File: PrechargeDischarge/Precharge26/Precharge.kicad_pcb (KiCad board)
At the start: 2 copper layers, 133 x 98 mm, 121 parts, among them J1 MicroFit, J2 Mini-Fit_Jr_5566-04A, J3 Micro-Fit 43045-0212, K1 OMRON-G2RL-24, K2 G7L-2A-X-L, Q1 2N7002, Q2 MMBT3906, Q3 2N7002, U1 TJA1051T-3, U10 LM393, U11 4N35, U2 SPAN02A-12, U3 Teensy4.0, U4 LM1117-5.0, U5 4N35, U6 4N35, U7 LM331, U8 LM331, U9 LM2904

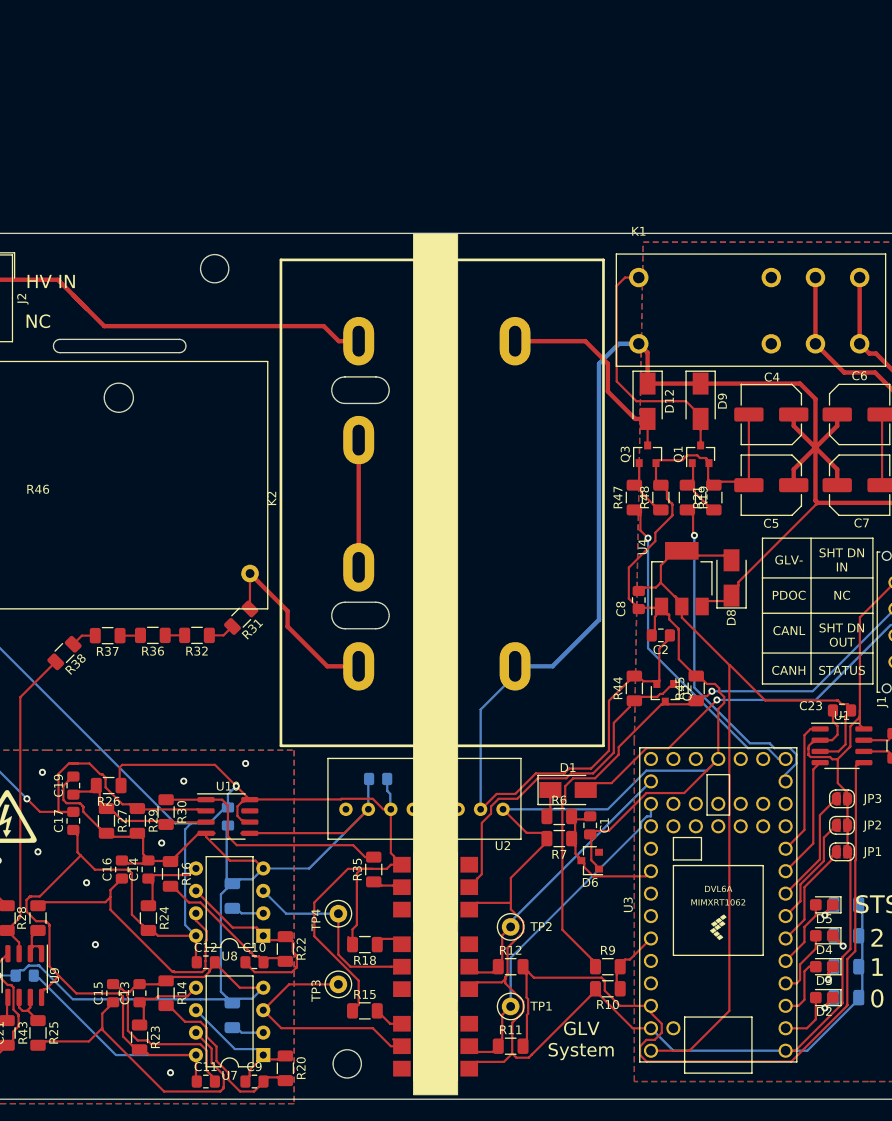
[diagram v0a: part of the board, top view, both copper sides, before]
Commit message: Precharge
Fixed Ground plane distance, added new DC converter, fixed precharge resistor value
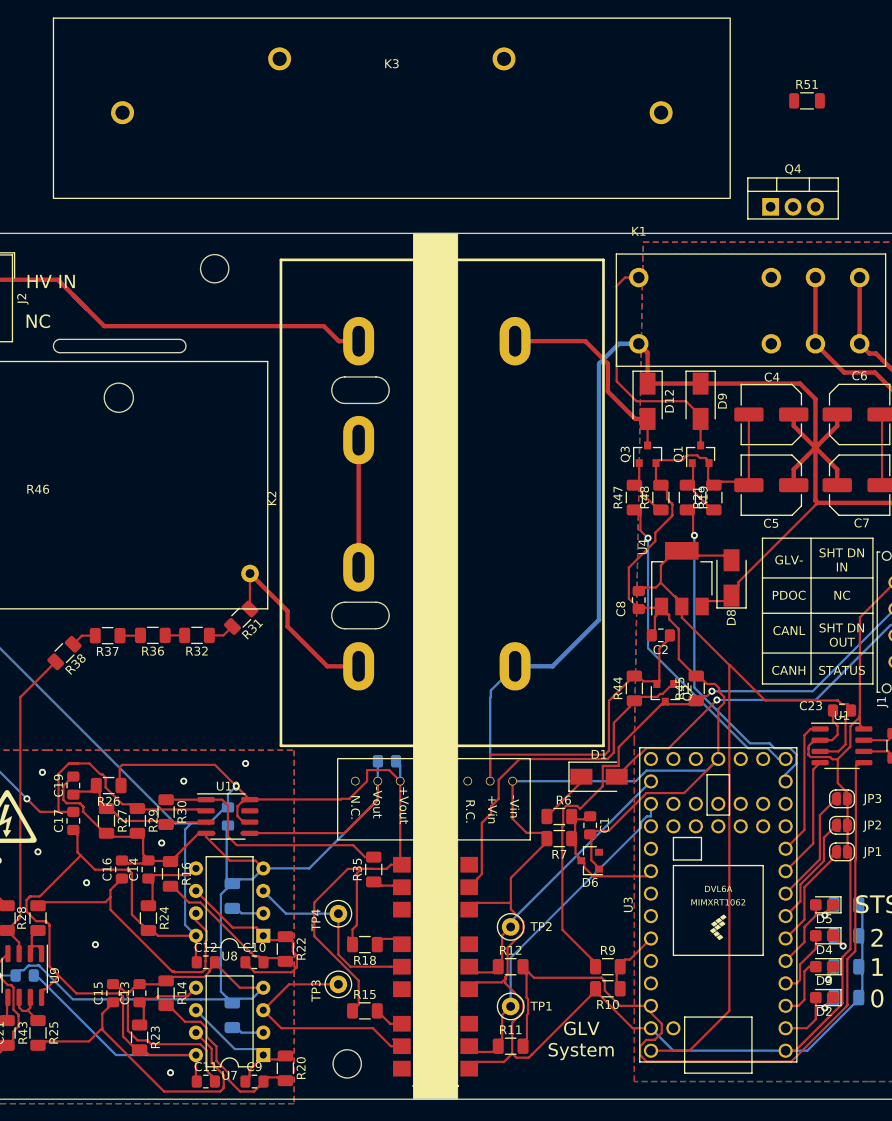
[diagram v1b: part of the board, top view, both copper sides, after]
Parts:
- added K3: Relay_SPST-NC, Library:Relay_SPST_NC_COMUS, F.Cu at (137.1, 36.3)
- added Q4: PMOS, Package_TO_SOT_THT:TO-220-3_Vertical, F.Cu at (179.9, 47.5)
- added R51: 10k, Resistor_SMD:R_1206_3216Metric, F.Cu at (184.0, 35.5)
- R46: value HSA25390RJ -> HSA253K3J
- U2: footprint Precharge:SPAN02 -> Precharge:DC-DCSPAN02W8-12
- moved D1 3.81 mm to (160.5, 112.0)
- moved C3 2.24 mm to (136.5, 110.2)
- moved U2 0.82 mm to (141.8, 114.5)
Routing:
- net GNDS: track 361.4 -> 367.4 mm
- net +12P: track 237.7 -> 242.4 mm
- net GLV+: track 92.4 -> 88.4 mm
- net +12V: track 188.0 -> 184.8 mm
- net Net-(D1-K): track 3.09 -> 6.12 mm
- net Net-(Q2-B): track 38.6 -> 39.9 mm
- net /PDOC_OK: track 68.3 -> 69.4 mm
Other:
- board text added: "5.0mm"

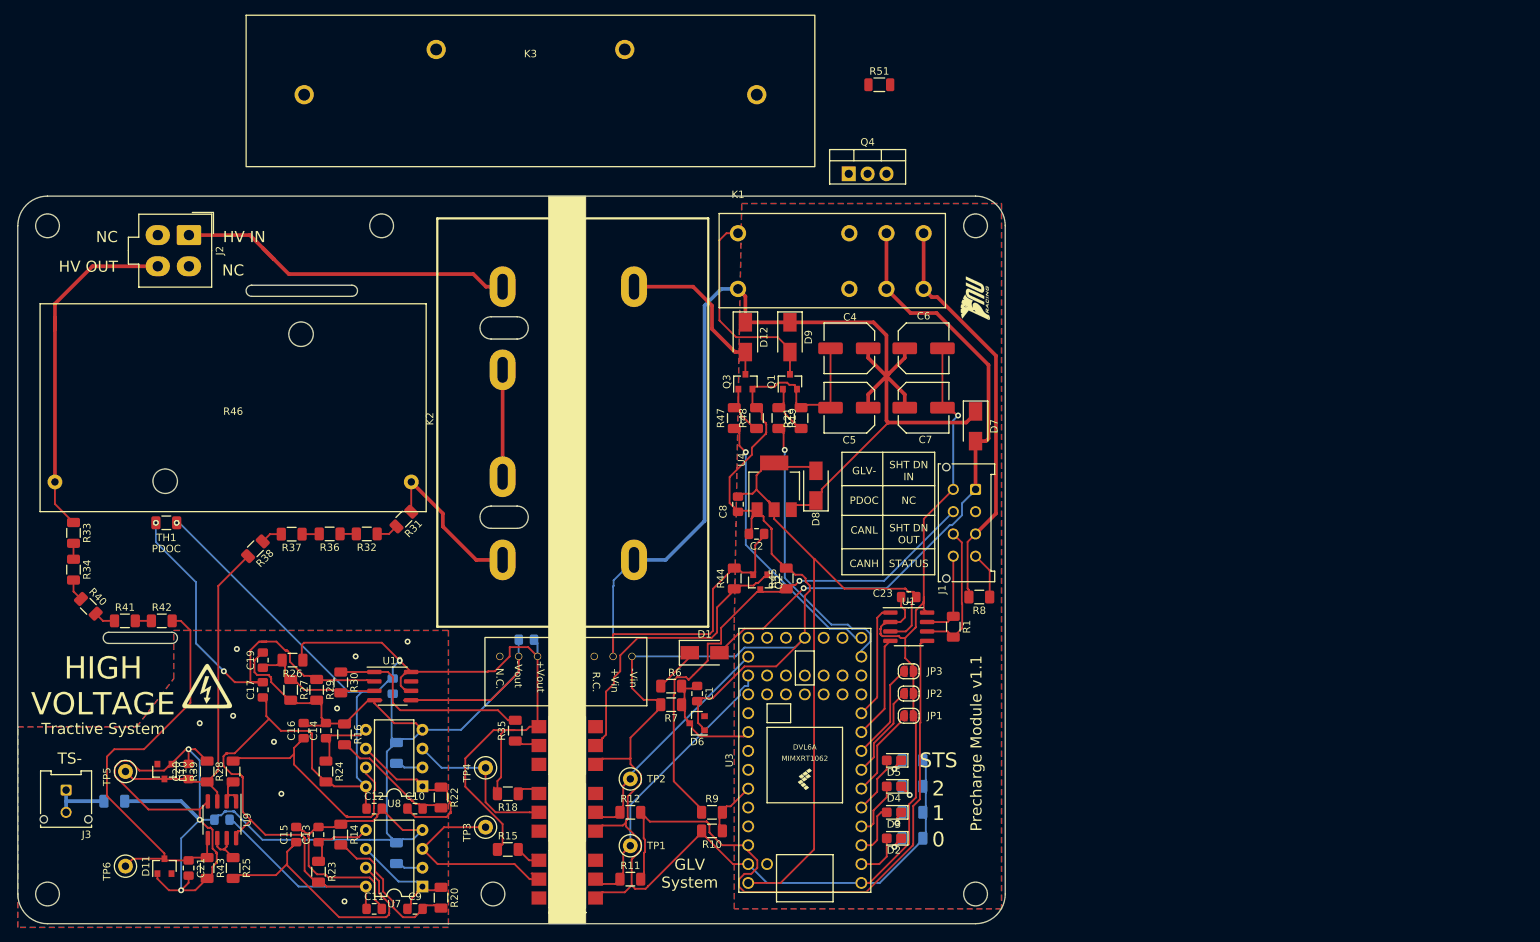
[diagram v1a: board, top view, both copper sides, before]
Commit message: added discharge relay and resistor footprints to precharge board
still need all part numbers but ffootprints are selected, go shopping on JLC
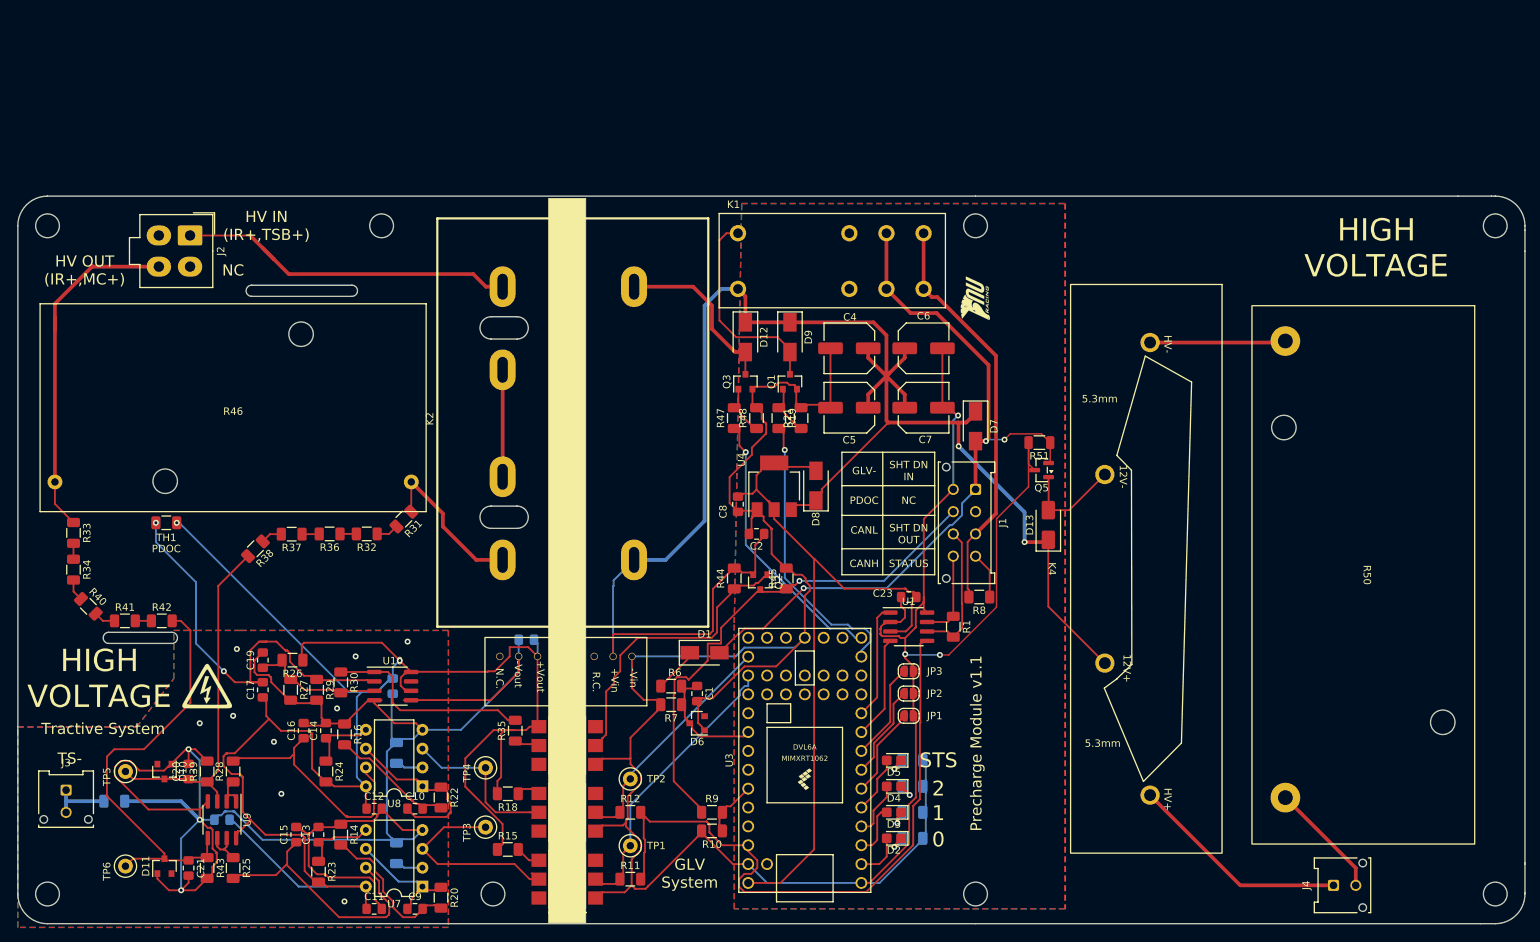
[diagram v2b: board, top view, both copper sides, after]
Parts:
- removed K3: Relay_SPST-NC, Library:Relay_SPST_NC_COMUS
- removed Q4: PMOS, Package_TO_SOT_THT:TO-220-3_Vertical
- added ?: , , F.Cu at (267.0, 144.5)
- added ?: , , F.Cu at (267.0, 54.5)
- added D13: D, Diode_SMD:D_SMA, F.Cu at (206.8, 94.8)
- added J4: Micro-Fit 43045-0212, Connector_Molex:Molex_Micro-Fit_3.0_43045-0212_2x01_P3.00mm_Vertical, F.Cu at (245.2, 143.3)
- added K4: Relay_SPST-NC, Precharge:Discharge_relay, F.Cu at (218.8, 100.7)
- added Q5: NMOS, Package_TO_SOT_SMD:SOT-23, F.Cu at (205.9, 87.4)
- added R50: HSA503K0J, Precharge:Discharge_Resistor, F.Cu at (249.2, 101.5)
- moved R51 52.8 mm to (205.6, 83.7), turned to 180 degrees
- moved J2 0.16 mm to (91.9, 55.8)
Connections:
- J1 pad 2: (no net) -> unconnected-(J1-Pin_2-Pad2)
- J2 pad 1: Net-(J2-Pad1) -> Net-(J2-Pin_1)
- J2 pad 2: (no net) -> unconnected-(J2-Pin_2-Pad2)
- J2 pad 3: (no net) -> unconnected-(J2-Pin_3-Pad3)
- K2 pad 8: unconnected-(K2-Pad8) -> Net-(J2-Pin_1)
- R51 pad 1: /SHUTDOWN -> GLV+
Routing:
- net Net-(J2-Pad1): track 47.3 -> 0.00 mm
- net Net-(J2-Pin_1): track 0.00 -> 47.1 mm
- net GLV-: track 321.8 -> 364.8 mm, vias 1 -> 3
- net +12V: track 184.8 -> 227.7 mm, vias 0 -> 2
- net /IR+_MC: track 0.00 -> 29.7 mm
- net Net-(K4-Pad4): track 0.00 -> 18.3 mm
- net /MSD_IN: track 0.00 -> 15.7 mm
- net Net-(D13-A): track 0.00 -> 14.1 mm
- net GLV+: track 88.4 -> 100.5 mm, vias 1 -> 3
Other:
- board size 133 x 98 mm -> 203 x 98 mm
- board text added: "5.3mm"
- board text added: "HV IN (IR+,TSB+)"
- board text added: "HV OUT (IR+,MC+)"
- board text removed: "HV IN"
- board text removed: "HV OUT"

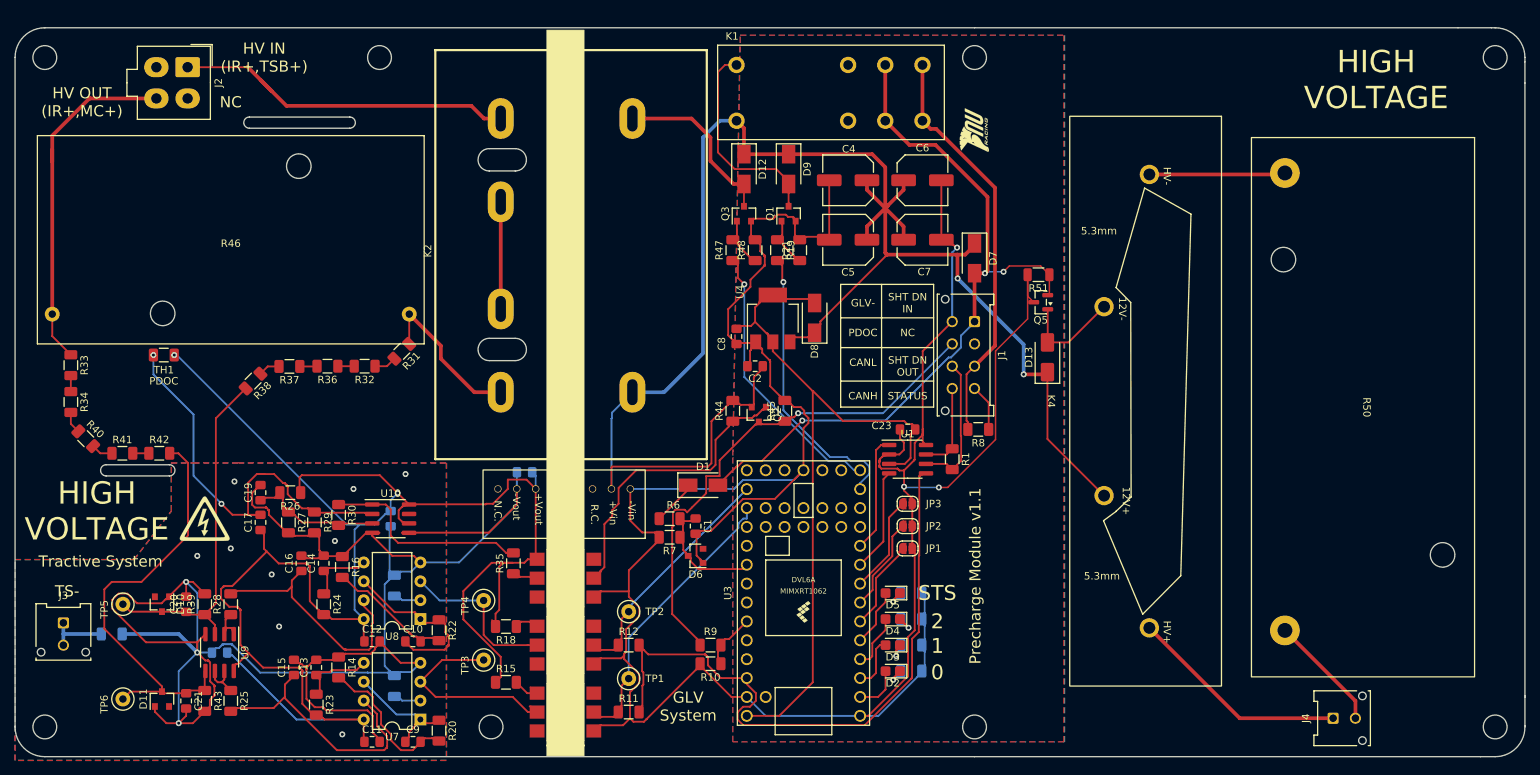
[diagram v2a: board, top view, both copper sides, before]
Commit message: precharge
fixed board edges
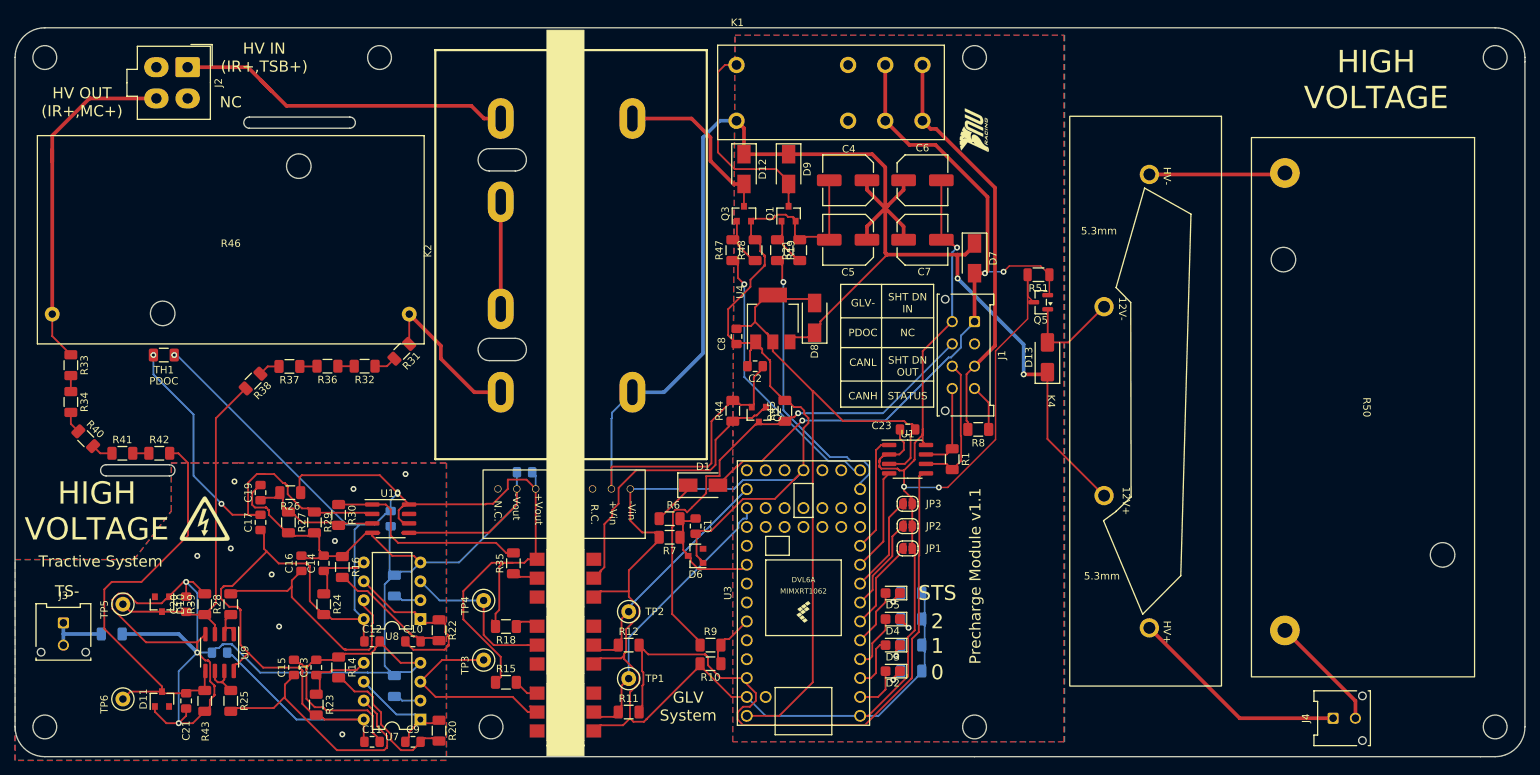
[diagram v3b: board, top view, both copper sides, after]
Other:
- outline, holes or cut-outs redrawn
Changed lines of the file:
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@@
 		(at 165 63)
 		(property "Reference" "K1"
-			(at -0.6 -11.36 0)
+			(at 0.1 -13.2 0)
 			(layer "F.SilkS")
 			(effects
@@
 		(tags "capacitor handsolder")
 		(property "Reference" "C21"
-			(at 0 -1.65 90)
+			(at 4 0 90)
 			(layer "F.SilkS")
 			(effects
@@
 		(tags "resistor")
 		(property "Reference" "R43"
-			(at 0 -1.82 90)
+			(at 4.1 -0.1 90)
 			(layer "F.SilkS")
 			(effects
@@
 	)
 	(gr_line
-		(start 271 144.47)
-		(end 271 144.33)
-		(stroke
-			(width 0.05)
-			(type default)
-		)
-		(layer "Edge.Cuts")
-	)
-	(gr_line
 		(start 197 148.5)
 		(end 265 148.5)
@@
 	)
 	(gr_line
-		(start 271 57.915786)
-		(end 271 140.5)
-		(stroke
-			(width 0.05)
-			(type default)
-		)
-		(layer "Edge.Cuts")
-	)
-	(gr_line
-		(start 271 140.3)
-		(end 271 144.33)
+		(start 271 55.08)
+		(end 271 144.47)
 		(stroke
 			(width 0.05)
@@
 	)
 	(gr_line
-		(start 197 50.5)
+		(start 267 50.5)
 		(end 72 50.5)
 		(stroke
@@
 		(layer "Edge.Cuts")
 	)
-	(gr_line
-		(start 271 57.915786)
-		(end 271 55.084213)
-		(stroke
-			(width 0.05)
-			(type default)
-		)
-		(layer "Edge.Cuts")
-	)
 	(gr_arc
 		(start 88.75 109.25)
@@
 		(layer "Edge.Cuts")
 	)
-	(gr_line
-		(start 262 50.5)
-		(end 266.48 50.5)
-		(stroke
-			(width 0.05)
-			(type default)
-		)
-		(layer "Edge.Cuts")
-	)
 	(gr_arc
 		(start 80.25 110.75)
@@
 	)
 	(gr_line
-		(start 266.48 50.5)
-		(end 267 50.5)
-		(stroke
-			(width 0.05)
-			(type default)
-		)
-		(layer "Edge.Cuts")
-	)
-	(gr_line
 		(start 68 54.5)
 		(end 68 144.5)
@@
 		(layer "Edge.Cuts")
 	)
-	(gr_line
-		(start 197 50.5)
-		(end 262 50.5)
-		(stroke
-			(width 0.05)
-			(type default)
-		)
-		(layer "Edge.Cuts")
-	)
 	(gr_arc
 		(start 135.25 92.25)
@@
 	)
 	(segment
-		(start 168.099 87.4838)
-		(end 167.4964 88.0864)
-		(width 0.25)
-		(layer "F.Cu")
-		(net 2)
-	)
-	(segment
 		(start 171.774 86.966)
 		(end 171.649 86.966)
@@
 	)
 	(segment
-		(start 167.4964 88.0864)
-		(end 167.4964 90.0368)
-		(width 0.25)
-		(layer "F.Cu")
-		(net 2)
-	)
-	(segment
 		(start 175.25 99.3578)
 		(end 175.3043 99.3578)
@@
 	)
 	(segment
-		(start 168.099 87.432)
-		(end 168.099 87.4838)
+		(start 188.402 108.348)
+		(end 187.615 109.135)
 		(width 0.25)
 		(layer "F.Cu")
@@
 	)
 	(segment
-		(start 188.402 108.348)
-		(end 187.615 109.135)
+		(start 167.4964 88.0864)
+		(end 167.4964 90.0368)
 		(width 0.25)
 		(layer "F.Cu")
@@
 	)
 	(segment
+		(start 169.874 86.432)
+		(end 169.1508 86.432)
+		(width 0.25)
+		(layer "F.Cu")
+		(net 2)
+	)
+	(segment
 		(start 187.5197 103.3778)
 		(end 187.5253 103.3834)
@@
 	)
 	(segment
-		(start 168.099 87.307)
-		(end 168.099 87.432)
-		(width 0.25)
-		(layer "F.Cu")
-		(net 2)
-	)
-	(segment
 		(start 169.0666 91.607)
 		(end 169.1758 91.607)
@@
 	)
 	(segment
+		(start 169.1508 86.432)
+		(end 167.4964 88.0864)
+		(width 0.25)
+		(layer "F.Cu")
+		(net 2)
+	)
+	(segment
 		(start 188.6353 103.8085)
 		(end 189.025 104.5)
@@
 	)
 	(segment
-		(start 169.874 86.432)
-		(end 168.099 87.307)
-		(width 0.25)
-		(layer "F.Cu")
-		(net 2)
-	)
-	(segment
 		(start 175.25 138.5)
 		(end 170.74 143.01)
@@
 	)
 	(segment
-		(start 73 65)
-		(end 73 68.5)
+		(start 78.05 59.95)
+		(end 73 65)
 		(width 0.5)
 		(layer "F.Cu")
@@
 	)
 	(segment
-		(start 78.05 59.95)
-		(end 78.1 60)
+		(start 78.1 60)
+		(end 78.05 59.95)
 		(width 0.5)
 		(layer "F.Cu")
@@
 	)
 	(segment
-		(start 73 66.85)
-		(end 73 68.5)
+		(start 87 60)
+		(end 78.1 60)
 		(width 0.5)
 		(layer "F.Cu")
@@
 	)
 	(segment
-		(start 78.05 59.95)
-		(end 73 65)
+		(start 73 66.85)
+		(end 73 68.5)
 		(width 0.5)
 		(layer "F.Cu")
@@
 	)
 	(segment
-		(start 78.1 60)
-		(end 87 60)
+		(start 73 65)
+		(end 73 68.5)
 		(width 0.5)
 		(layer "F.Cu")
@@
 		(start 91.2 55.8)
 		(end 99.2 55.8)
-		(width 0.25)
+		(width 0.5)
 		(layer "F.Cu")
 		(net 91)
@@
 		(polygon
 			(pts
-				(xy 164.5 146.5) (xy 164.5 108) (xy 165.5 51.5) (xy 209 51.5) (xy 209 146.5) (xy 191 146.5)
+				(xy 164.5 146.5) (xy 164.5 108) (xy 164.8 51.5) (xy 209 51.5) (xy 209 146.5) (xy 191 146.5)
 			)
 		)
@@
 		(polygon
 			(pts
-				(xy 164.5 146.5) (xy 164.5 108) (xy 165.5 51.5) (xy 209.1 51.5) (xy 209.1 146.5) (xy 191 146.5)
+				(xy 164.5 146.5) (xy 164.5 108) (xy 164.8 51.5) (xy 209.1 51.5) (xy 209.1 146.5) (xy 191 146.5)
 			)
 		)
